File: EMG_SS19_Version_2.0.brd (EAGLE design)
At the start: 160 x 100 mm, 219 parts, among them T11 OPA388, T12 OPA388, T21 OPA388, T22 OPA388

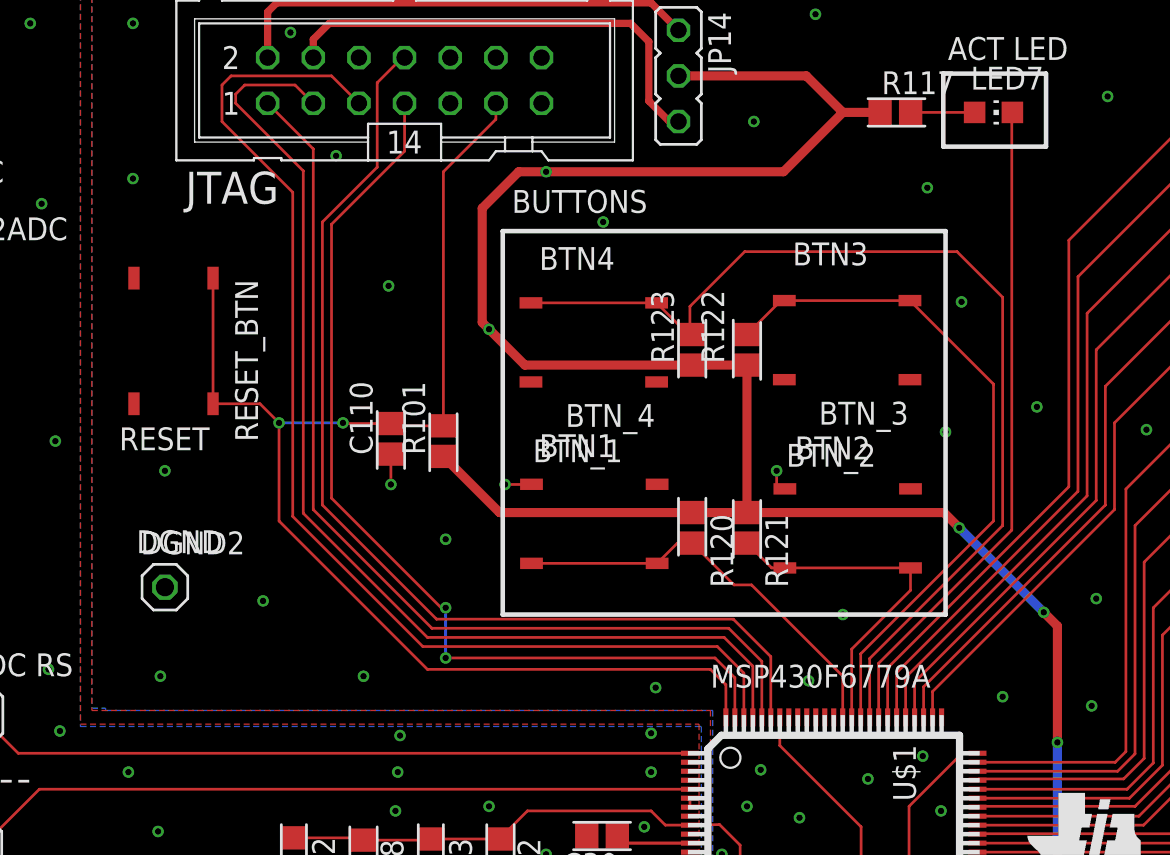
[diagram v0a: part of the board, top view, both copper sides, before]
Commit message: buttons replaced, addad some labeling
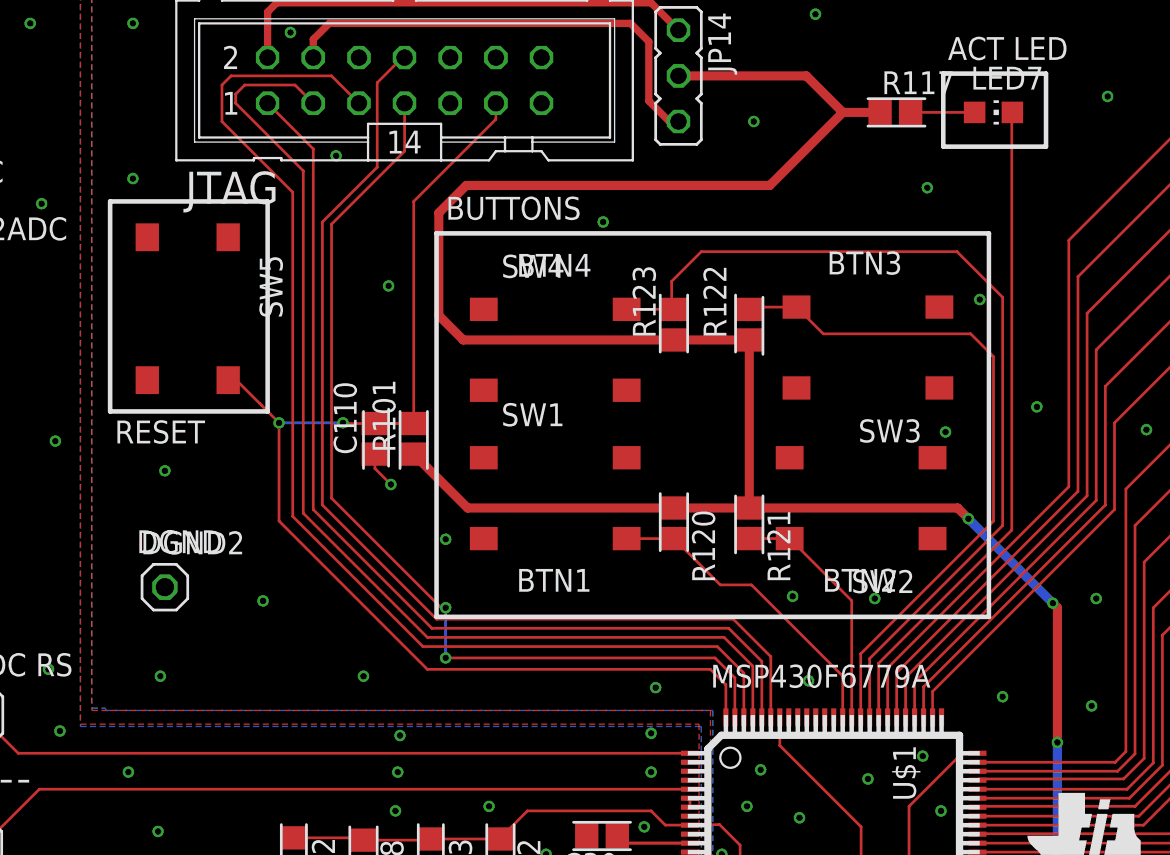
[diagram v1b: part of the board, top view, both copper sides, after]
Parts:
- removed BTN_1, BTN_2, BTN_3, BTN_4, RESET_BTN: PUSH-BUTTONSURFACE-MOUNT, Taster:HDKJ
- added SW1, SW2, SW3, SW4, SW5: B3S-1000, B3S-1000:SW_B3S-1000
- moved R123 1.73 mm to (122.7, 80.6)
- moved R101 1.66 mm to (108.2, 74.3)
- moved R122 1.40 mm to (126.9, 80.6)
- moved R120 1.05 mm to (122.7, 69.6)
- moved C110 0.89 mm to (106.0, 74.3)
- moved R121 0.28 mm to (126.9, 69.6)
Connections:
- new net N$56: SW2.1
- net BTN1: now also SW1.1; no longer BTN_1.OU1, BTN_1.OUT2
- net BTN2: now also SW2.3; no longer BTN_2.OU1, BTN_2.OUT2
- net BTN3: now also SW3.1; no longer BTN_3.OU1, BTN_3.OUT2
- net BTN4: now also SW4.3; no longer BTN_4.OU1, BTN_4.OUT2
- net DGND: now also SW1.4, SW2.4, SW3.4, SW4.4, SW5.4; no longer BTN_1.IN1, BTN_1.IN2, BTN_2.IN1, BTN_2.IN2, BTN_3.IN1, BTN_3.IN2, BTN_4.IN1, BTN_4.IN2, RESET_BTN.OU1, RESET_BTN.OUT2
- net RESET: now also SW5.3; no longer RESET_BTN.IN1, RESET_BTN.IN2
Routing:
- net RESET: track 75.4 -> 66.9 mm
- net DVCC: track 283.3 -> 290.8 mm, vias 8 -> 6
- net BTN4: track 57.4 -> 50.9 mm
- net BTN2: track 19.3 -> 13.6 mm
- net BTN1: track 23.1 -> 17.5 mm
- net DGND: track 15.6 -> 12.7 mm, vias 93 -> 92

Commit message: few small details
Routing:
- net DGND: vias 92 -> 99
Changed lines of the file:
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@@
 <layer number="14" name="Route14" color="22" fill="1" visible="no" active="no"/>
 <layer number="15" name="Route15" color="23" fill="1" visible="no" active="no"/>
-<layer number="16" name="Bottom" color="1" fill="1" visible="no" active="yes"/>
+<layer number="16" name="Bottom" color="1" fill="1" visible="yes" active="yes"/>
 <layer number="17" name="Pads" color="2" fill="1" visible="yes" active="yes"/>
 <layer number="18" name="Vias" color="2" fill="1" visible="yes" active="yes"/>
@@
 <layer number="20" name="Dimension" color="24" fill="1" visible="yes" active="yes"/>
 <layer number="21" name="tPlace" color="16" fill="1" visible="yes" active="yes"/>
-<layer number="22" name="bPlace" color="7" fill="1" visible="yes" active="yes"/>
-<layer number="23" name="tOrigins" color="15" fill="1" visible="yes" active="yes"/>
-<layer number="24" name="bOrigins" color="15" fill="1" visible="yes" active="yes"/>
+<layer number="22" name="bPlace" color="7" fill="1" visible="no" active="yes"/>
+<layer number="23" name="tOrigins" color="15" fill="1" visible="no" active="yes"/>
+<layer number="24" name="bOrigins" color="15" fill="1" visible="no" active="yes"/>
 <layer number="25" name="tNames" color="7" fill="1" visible="no" active="yes"/>
 <layer number="26" name="bNames" color="7" fill="1" visible="no" active="yes"/>
@@
 <via x="140.97" y="59.944" extent="1-16" drill="0.35"/>
 <via x="142.875" y="76.073" extent="1-16" drill="0.35"/>
-<via x="137.795" y="74.676" extent="1-16" drill="0.35"/>
+<via x="138.938" y="75.184" extent="1-16" drill="0.35"/>
 <via x="139.7" y="82.042" extent="1-16" drill="0.35"/>
 <via x="136.779" y="88.265" extent="1-16" drill="0.35"/>
@@
 <contactref element="SW4" pad="4"/>
 <contactref element="SW5" pad="4"/>
-<via x="129.286" y="65.532" extent="1-16" drill="0.35"/>
+<via x="129.159" y="66.294" extent="1-16" drill="0.35"/>
+<via x="123.952" y="74.295" extent="1-16" drill="0.35"/>
+<via x="133.477" y="76.962" extent="1-16" drill="0.35"/>
+<via x="132.969" y="73.279" extent="1-16" drill="0.35"/>
+<via x="115.951" y="73.406" extent="1-16" drill="0.35"/>
+<via x="115.951" y="67.31" extent="1-16" drill="0.35"/>
+<via x="117.094" y="82.931" extent="1-16" drill="0.35"/>
+<via x="106.426" y="80.01" extent="1-16" drill="0.35"/>
 </signal>
 <signal name="N$61">
